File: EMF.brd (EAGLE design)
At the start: 49.2 x 63.5 mm, 23 parts, among them X1 22-23-2021

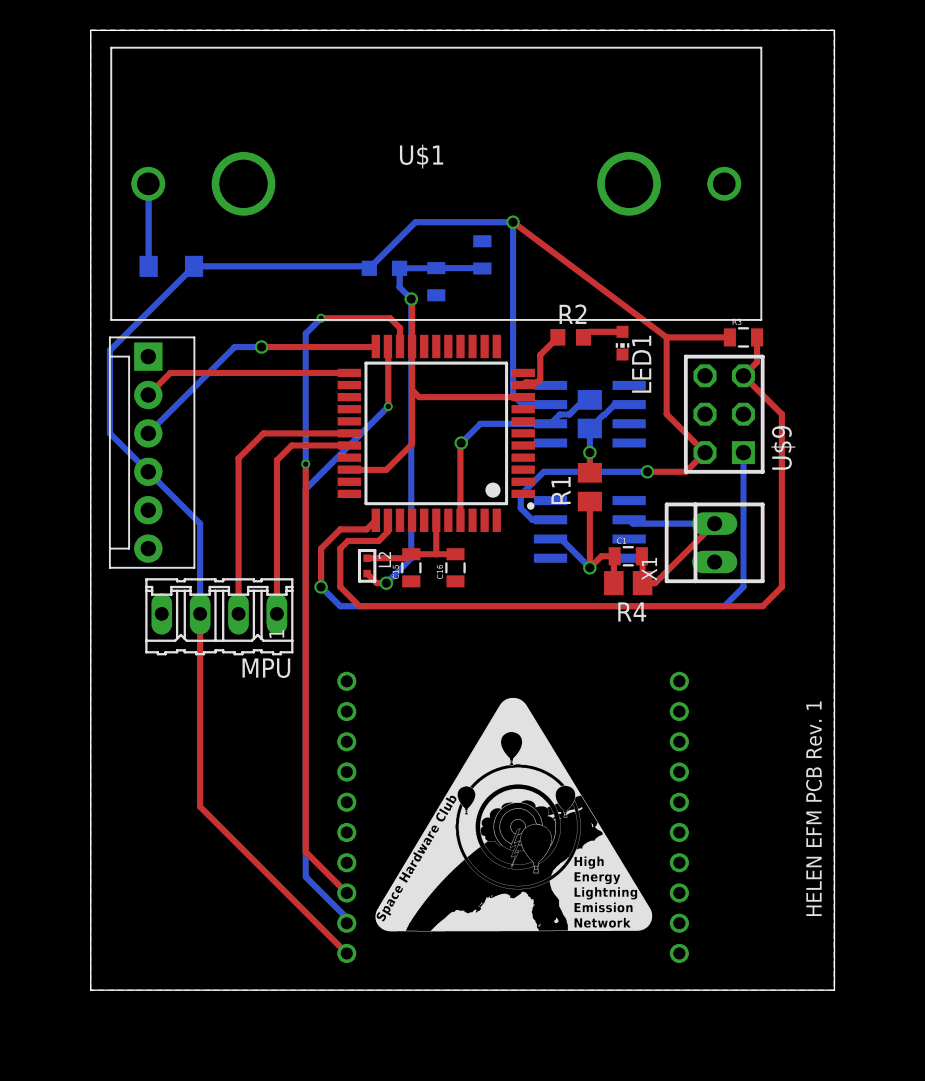
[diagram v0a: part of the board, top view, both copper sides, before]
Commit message: Make fixes, remove XBEE, add screw holes
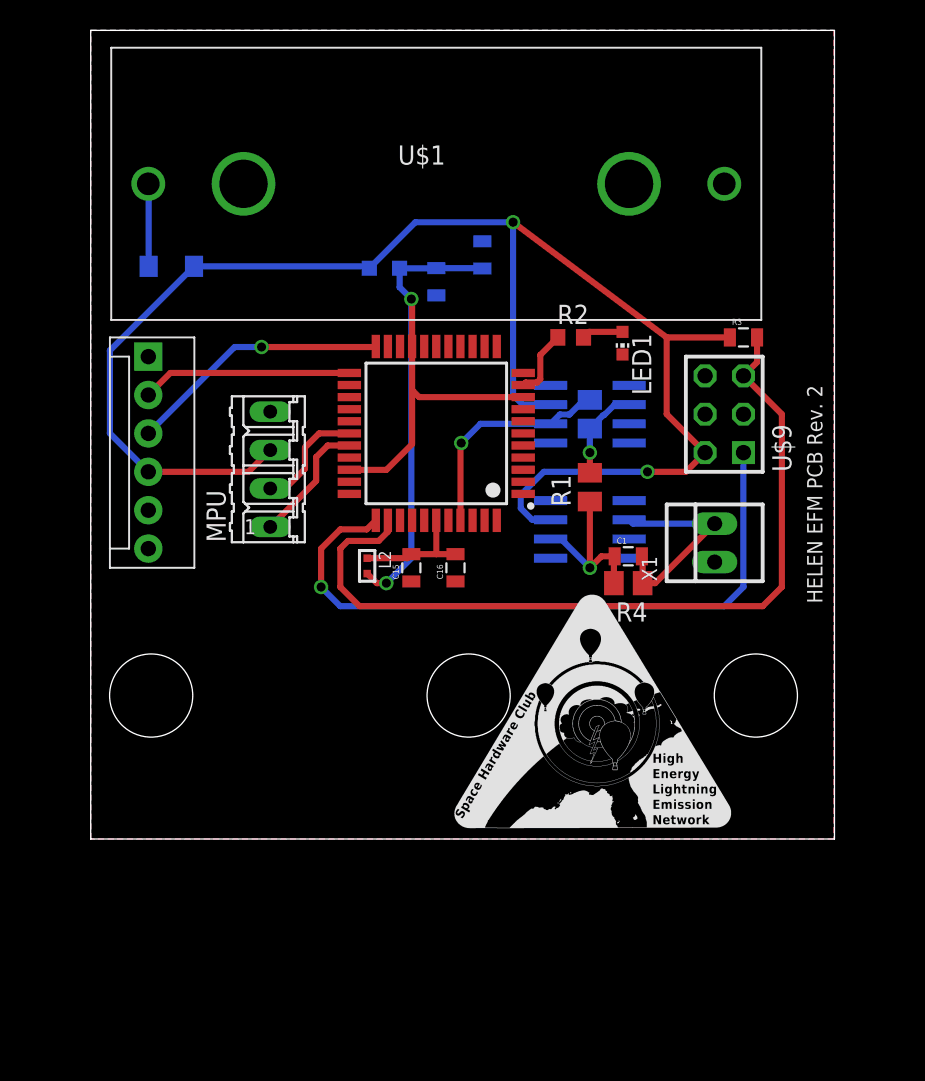
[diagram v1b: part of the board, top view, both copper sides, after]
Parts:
- removed XB1: XBEE, maxstream:XBEE
- moved MPU 10.1 mm to (11.9, 51.0), turned to 90 degrees
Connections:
- net GND: no longer XB1.10
- net V+: no longer XB1.1
- net XBIN: no longer XB1.3
- net XBOUT: no longer XB1.2
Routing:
- net XBIN: track 46.3 -> 0.00 mm, vias 2 -> 0
- net XBOUT: track 41.5 -> 0.00 mm, vias 1 -> 0
- net V+: track 132.9 -> 104.3 mm
- net SDAD: track 18.3 -> 7.56 mm
- net SCLE: track 15.4 -> 8.39 mm
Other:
- board size 49.2 x 63.5 mm -> 49.2 x 53.5 mm
- board text added: "HELEN EFM PCB Rev. 2"
- board text removed: "HELEN EFM PCB Rev. 1"
